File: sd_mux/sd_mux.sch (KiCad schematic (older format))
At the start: 16 parts, among them IC1 SN74CBT3257DR, IC2 SN74CBT3257DR, J1 Micro_SD_Card_Det, J2 DEVICE 1, J3 DEVICE 2, J4 CONTROL

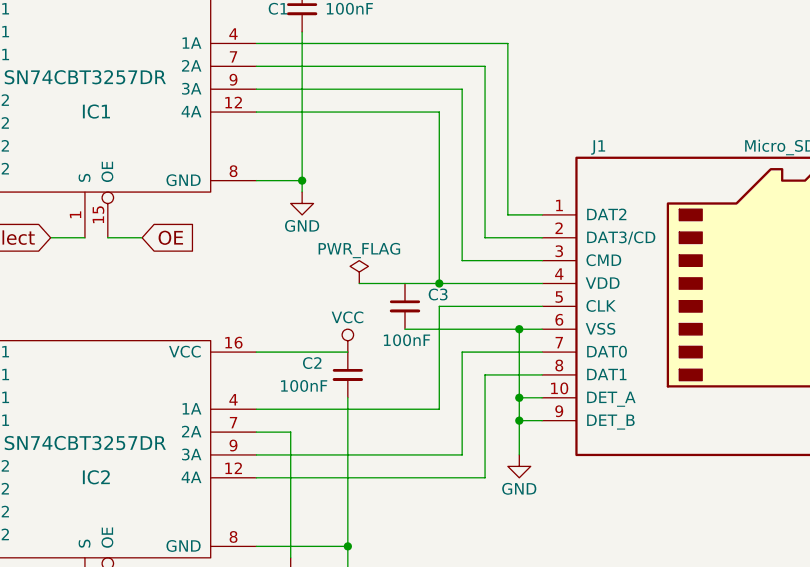
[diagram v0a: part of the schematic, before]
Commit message: added readme, generated netlist
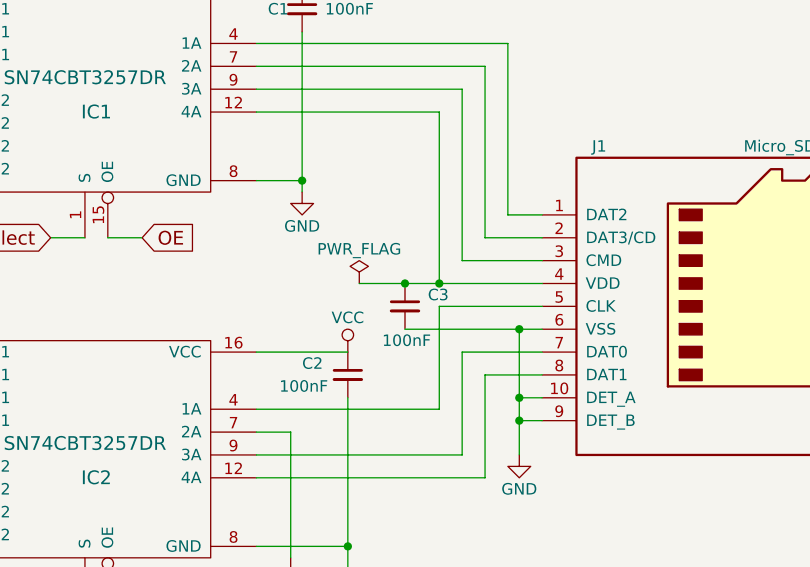
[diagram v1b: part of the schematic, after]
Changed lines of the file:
@@
 	7050 2450 6150 2450
+Wire Wire Line
+	6600 3300 6800 3300
 Wire Wire Line
 	6800 3300 6950 3300
@@
 $EndComp
 Wire Wire Line
-	6600 3300 6800 3300
+	6800 3300 6800 3300
+Connection ~ 6800 3300
 $EndSCHEMATC

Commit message: first attempt at routing sd_mux
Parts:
- C1, C2, C3: footprint (none) -> Capacitors_SMD:C_0603_HandSoldering
- IC1, IC2: footprint (none) -> SMD_Packages:SO-16-N
- J1: footprint (none) -> sd_mux_footprints:push_pull_uSD_slot_1040310811
- J2, J3: footprint (none) -> sd_mux_footprints:FFC_connector_SFW12R-2STE1LF
- J4: footprint (none) -> Pin_Headers:Pin_Header_Straight_1x03_Pitch2.54mm
- LED1, LED2: footprint (none) -> LEDs:LED_0603_HandSoldering
- R1, R2, R3, R4, R5: footprint (none) -> Resistors_SMD:R_0603_HandSoldering
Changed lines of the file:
@@
 F 0 "J1" H 7650 4100 50  0000 C CNN
 F 1 "Micro_SD_Card_Det" H 8950 4100 50  0000 R CNN
-F 2 "" H 10350 4100 50  0001 C CNN
+F 2 "sd_mux_footprints:push_pull_uSD_slot_1040310811" H 10350 4100 50  0001 C CNN
 F 3 "" H 8300 3500 50  0001 C CNN
 	1    8300 3400
@@
 F 0 "IC1" H 5450 2250 60  0000 C CNN
 F 1 "SN74CBT3257DR" H 5400 2400 60  0000 C CNN
-F 2 "" H 5300 2250 60  0001 C CNN
+F 2 "SMD_Packages:SO-16-N" H 5300 2250 60  0001 C CNN
 F 3 "" H 5300 2250 60  0001 C CNN
 	1    5450 2400
@@
 F 0 "IC2" H 5450 3850 60  0000 C CNN
 F 1 "SN74CBT3257DR" H 5400 4000 60  0000 C CNN
-F 2 "" H 5300 3850 60  0001 C CNN
+F 2 "SMD_Packages:SO-16-N" H 5300 3850 60  0001 C CNN
 F 3 "" H 5300 3850 60  0001 C CNN
 	1    5450 4000
@@
 F 0 "J2" H 2250 3000 50  0000 C CNN
 F 1 "DEVICE 1" H 2250 1700 50  0000 C CNN
-F 2 "" H 2250 2400 50  0001 C CNN
+F 2 "sd_mux_footprints:FFC_connector_SFW12R-2STE1LF" H 2250 2400 50  0001 C CNN
 F 3 "" H 2250 2400 50  0001 C CNN
 	1    2250 2400
@@
 F 0 "J3" H 2250 4800 50  0000 C CNN
 F 1 "DEVICE 2" H 2250 3500 50  0000 C CNN
-F 2 "" H 2250 4200 50  0001 C CNN
+F 2 "sd_mux_footprints:FFC_connector_SFW12R-2STE1LF" H 2250 4200 50  0001 C CNN
 F 3 "" H 2250 4200 50  0001 C CNN
 	1    2250 4200
@@
 F 0 "J4" H 8350 5950 50  0000 C CNN
 F 1 "CONTROL" H 8350 5550 50  0000 C CNN
-F 2 "" H 8350 5750 50  0001 C CNN
+F 2 "Pin_Headers:Pin_Header_Straight_1x03_Pitch2.54mm" H 8350 5750 50  0001 C CNN
 F 3 "" H 8350 5750 50  0001 C CNN
 	1    8350 5750
@@
 F 0 "R1" V 7980 5550 50  0000 C CNN
 F 1 "10K" V 7800 5550 50  0000 C CNN
-F 2 "" V 7830 5550 50  0001 C CNN
+F 2 "Resistors_SMD:R_0603_HandSoldering" V 7830 5550 50  0001 C CNN
 F 3 "" H 7900 5550 50  0001 C CNN
 	1    7900 5550
@@
 F 0 "R2" V 5830 4950 50  0000 C CNN
 F 1 "10K" V 5650 4950 50  0000 C CNN
-F 2 "" V 5680 4950 50  0001 C CNN
+F 2 "Resistors_SMD:R_0603_HandSoldering" V 5680 4950 50  0001 C CNN
 F 3 "" H 5750 4950 50  0001 C CNN
 	1    5750 4950
@@
 F 0 "R3" V 7030 5000 50  0000 C CNN
 F 1 "1K" V 6850 5000 50  0000 C CNN
-F 2 "" V 6880 5000 50  0001 C CNN
+F 2 "Resistors_SMD:R_0603_HandSoldering" V 6880 5000 50  0001 C CNN
 F 3 "" H 6950 5000 50  0001 C CNN
 	1    6950 5000
@@
 F 0 "R4" V 7030 5300 50  0000 C CNN
 F 1 "1K" V 6850 5300 50  0000 C CNN
-F 2 "" V 6880 5300 50  0001 C CNN
+F 2 "Resistors_SMD:R_0603_HandSoldering" V 6880 5300 50  0001 C CNN
 F 3 "" H 6950 5300 50  0001 C CNN
 	1    6950 5300
@@
 F 0 "C1" H 6200 2100 50  0000 L CNN
 F 1 "100nF" H 6450 2100 50  0000 L CNN
-F 2 "" H 6350 2100 50  0001 C CNN
+F 2 "Capacitors_SMD:C_0603_HandSoldering" H 6350 2100 50  0001 C CNN
 F 3 "" H 6350 2100 50  0001 C CNN
 	1    6350 2100
@@
 F 0 "C2" H 6350 3750 50  0000 L CNN
 F 1 "100nF" H 6250 3650 50  0000 L CNN
-F 2 "" H 6550 3700 50  0001 C CNN
+F 2 "Capacitors_SMD:C_0603_HandSoldering" H 6550 3700 50  0001 C CNN
 F 3 "" H 6550 3700 50  0001 C CNN
 	1    6550 3700
@@
 	6150 2850 6350 2850
 Wire Wire Line
-	6350 2200 6350 2850
-Wire Wire Line
-	6350 2850 6350 2900
+	6350 2200 6350 2900
 Wire Wire Line
 	6550 4450 6150 4450
 Wire Wire Line
-	6800 3500 7300 3500
-Wire Wire Line
-	7300 3500 7400 3500
+	6800 3500 7400 3500
 Wire Wire Line
 	9250 3900 9100 3900
@@
 	7050 2450 6150 2450
 Wire Wire Line
-	6600 3300 6800 3300
-Wire Wire Line
-	6800 3300 6950 3300
-Wire Wire Line
-	6950 3300 7400 3300
+	6600 3300 7400 3300
 Wire Wire Line
 	6950 3300 6950 2550
@@
 	7150 3700 7150 4150
 Wire Wire Line
-	6550 3800 6550 4450
-Wire Wire Line
-	6550 4450 6550 4950
-Wire Wire Line
-	6550 4950 6550 5000
-Wire Wire Line
-	7300 3500 7300 3800
-Wire Wire Line
-	7300 3800 7300 3900
-Wire Wire Line
-	7300 3900 7300 4050
+	6550 3800 6550 5000
+Wire Wire Line
+	7300 3500 7300 4050
 Wire Wire Line
 	7400 3800 7300 3800
@@
 	5400 4700 5250 4700
 Wire Wire Line
-	7350 5750 7650 5750
-Wire Wire Line
-	7650 5750 7900 5750
-Wire Wire Line
-	7900 5750 8150 5750
+	7350 5750 8150 5750
 Connection ~ 7900 5750
 Wire Wire Line
 	5650 3100 5500 3100
 Wire Wire Line
-	5500 4700 5550 4700
-Wire Wire Line
-	5550 4700 5650 4700
+	5500 4700 5650 4700
 Wire Wire Line
 	5550 4700 5550 4950
@@
 Connection ~ 6550 4450
 Wire Wire Line
-	5900 4950 6300 4950
-Wire Wire Line
-	6300 4950 6550 4950
+	5900 4950 6550 4950
 Connection ~ 6550 4950
 Connection ~ 7300 3900
@@
 	2600 3800 2450 3800
 Wire Wire Line
-	2600 2000 2600 2200
-Wire Wire Line
-	2600 2200 2600 2500
-Wire Wire Line
-	2600 2500 2600 2700
-Wire Wire Line
-	2600 2700 2600 2900
-Wire Wire Line
-	2600 2900 2600 3800
-Wire Wire Line
-	2600 3800 2600 4000
-Wire Wire Line
-	2600 4000 2600 4300
-Wire Wire Line
-	2600 4300 2600 4500
-Wire Wire Line
-	2600 4500 2600 4700
-Wire Wire Line
-	2600 4700 2600 5000
+	2600 2000 2600 5000
 Wire Wire Line
 	2600 4700 2450 4700
@@
 	8150 5850 8050 5850
 Wire Wire Line
-	8150 5250 8150 5300
-Wire Wire Line
-	8150 5300 8150 5650
+	8150 5250 8150 5650
 Connection ~ 8150 5300
 Wire Wire Line
@@
 	7200 5300 7100 5300
 Wire Wire Line
-	6700 5000 6700 5300
-Wire Wire Line
-	6700 5300 6700 5400
+	6700 5000 6700 5400
 Wire Wire Line
 	6700 5000 6800 5000
@@
 F 0 "C3" H 6900 3450 50  0000 L CNN
 F 1 "100nF" H 6700 3250 50  0000 L CNN
-F 2 "" H 6800 3400 50  0001 C CNN
+F 2 "Capacitors_SMD:C_0603_HandSoldering" H 6800 3400 50  0001 C CNN
 F 3 "" H 6800 3400 50  0001 C CNN
 	1    6800 3400
@@
 F 0 "LED1" H 7350 5100 50  0000 C CNN
 F 1 "PWR" H 7350 4900 50  0000 C CNN
-F 2 "" H 7350 5000 50  0001 C CNN
+F 2 "LEDs:LED_0603_HandSoldering" H 7350 5000 50  0001 C CNN
 F 3 "" H 7350 5000 50  0001 C CNN
 	1    7350 5000
@@
 F 0 "LED2" H 7350 5400 50  0000 C CNN
 F 1 "SEL" H 7350 5200 50  0000 C CNN
-F 2 "" H 7350 5300 50  0001 C CNN
+F 2 "LEDs:LED_0603_HandSoldering" H 7350 5300 50  0001 C CNN
 F 3 "" H 7350 5300 50  0001 C CNN
 	1    7350 5300
@@
 F 0 "R5" V 6380 4650 50  0000 C CNN
 F 1 "10K" V 6200 4650 50  0000 C CNN
-F 2 "" V 6230 4650 50  0001 C CNN
+F 2 "Resistors_SMD:R_0603_HandSoldering" V 6230 4650 50  0001 C CNN
 F 3 "" H 6300 4650 50  0001 C CNN
 	1    6300 4650

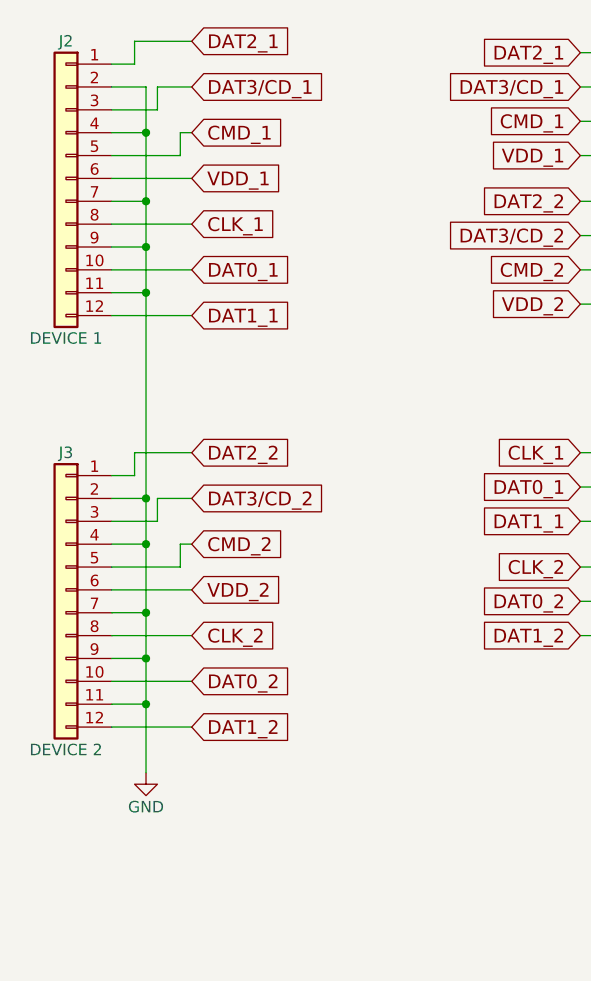
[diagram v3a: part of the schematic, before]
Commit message: rerouted mux board to fix FFC flip issue and fix tracks that had become unalaigned from the grid
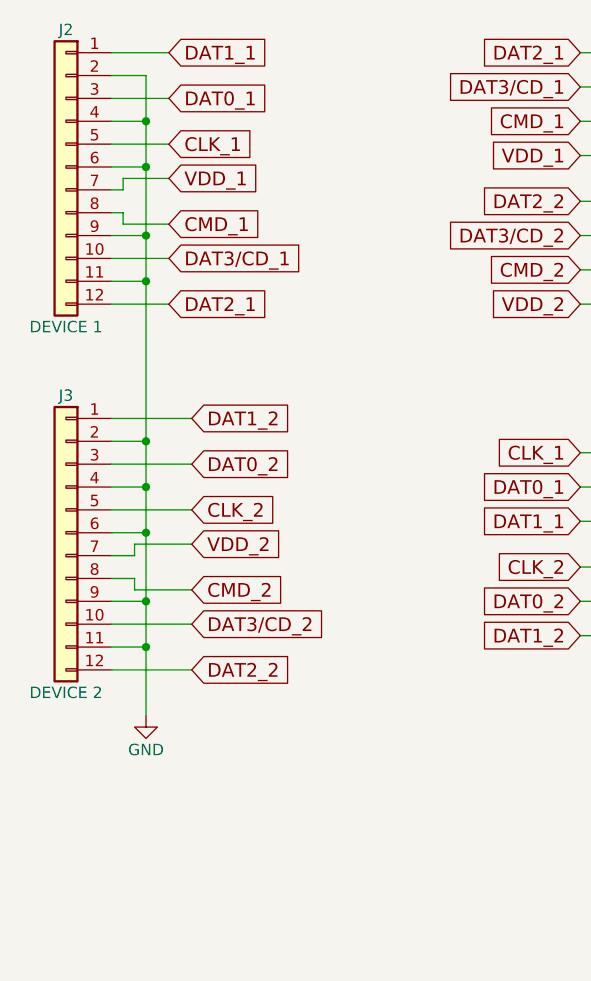
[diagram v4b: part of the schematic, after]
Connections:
- net CLK_1: now also J2.5 (Pin_5); no longer J2.8 (Pin_8)
- net CLK_2: now also J3.5 (Pin_5); no longer J3.8 (Pin_8)
- net CMD_1: now also J2.8 (Pin_8); no longer J2.5 (Pin_5)
- net CMD_2: now also J3.8 (Pin_8); no longer J3.5 (Pin_5)
- net DAT0_1: now also J2.3 (Pin_3); no longer J2.10 (Pin_10)
- net DAT0_2: now also J3.3 (Pin_3); no longer J3.10 (Pin_10)
- net DAT1_1: now also J2.1 (Pin_1); no longer J2.12 (Pin_12)
- net DAT1_2: now also J3.1 (Pin_1); no longer J3.12 (Pin_12)
- net DAT2_1: now also J2.12 (Pin_12); no longer J2.1 (Pin_1)
- net DAT2_2: now also J3.12 (Pin_12); no longer J3.1 (Pin_1)
- net DAT3/CD_1: now also J2.10 (Pin_10); no longer J2.3 (Pin_3)
- net DAT3/CD_2: now also J3.10 (Pin_10); no longer J3.3 (Pin_3)
- net GND: now also J2.6 (Pin_6), J3.6 (Pin_6); no longer J2.7 (Pin_7), J3.7 (Pin_7)
- net VDD_1: now also J2.7 (Pin_7); no longer J2.6 (Pin_6)
- net VDD_2: now also J3.7 (Pin_7); no longer J3.6 (Pin_6)
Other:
- moved on the sheet: J2, J3
